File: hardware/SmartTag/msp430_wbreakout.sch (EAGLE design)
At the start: 19 parts, among them U1 ADXL362

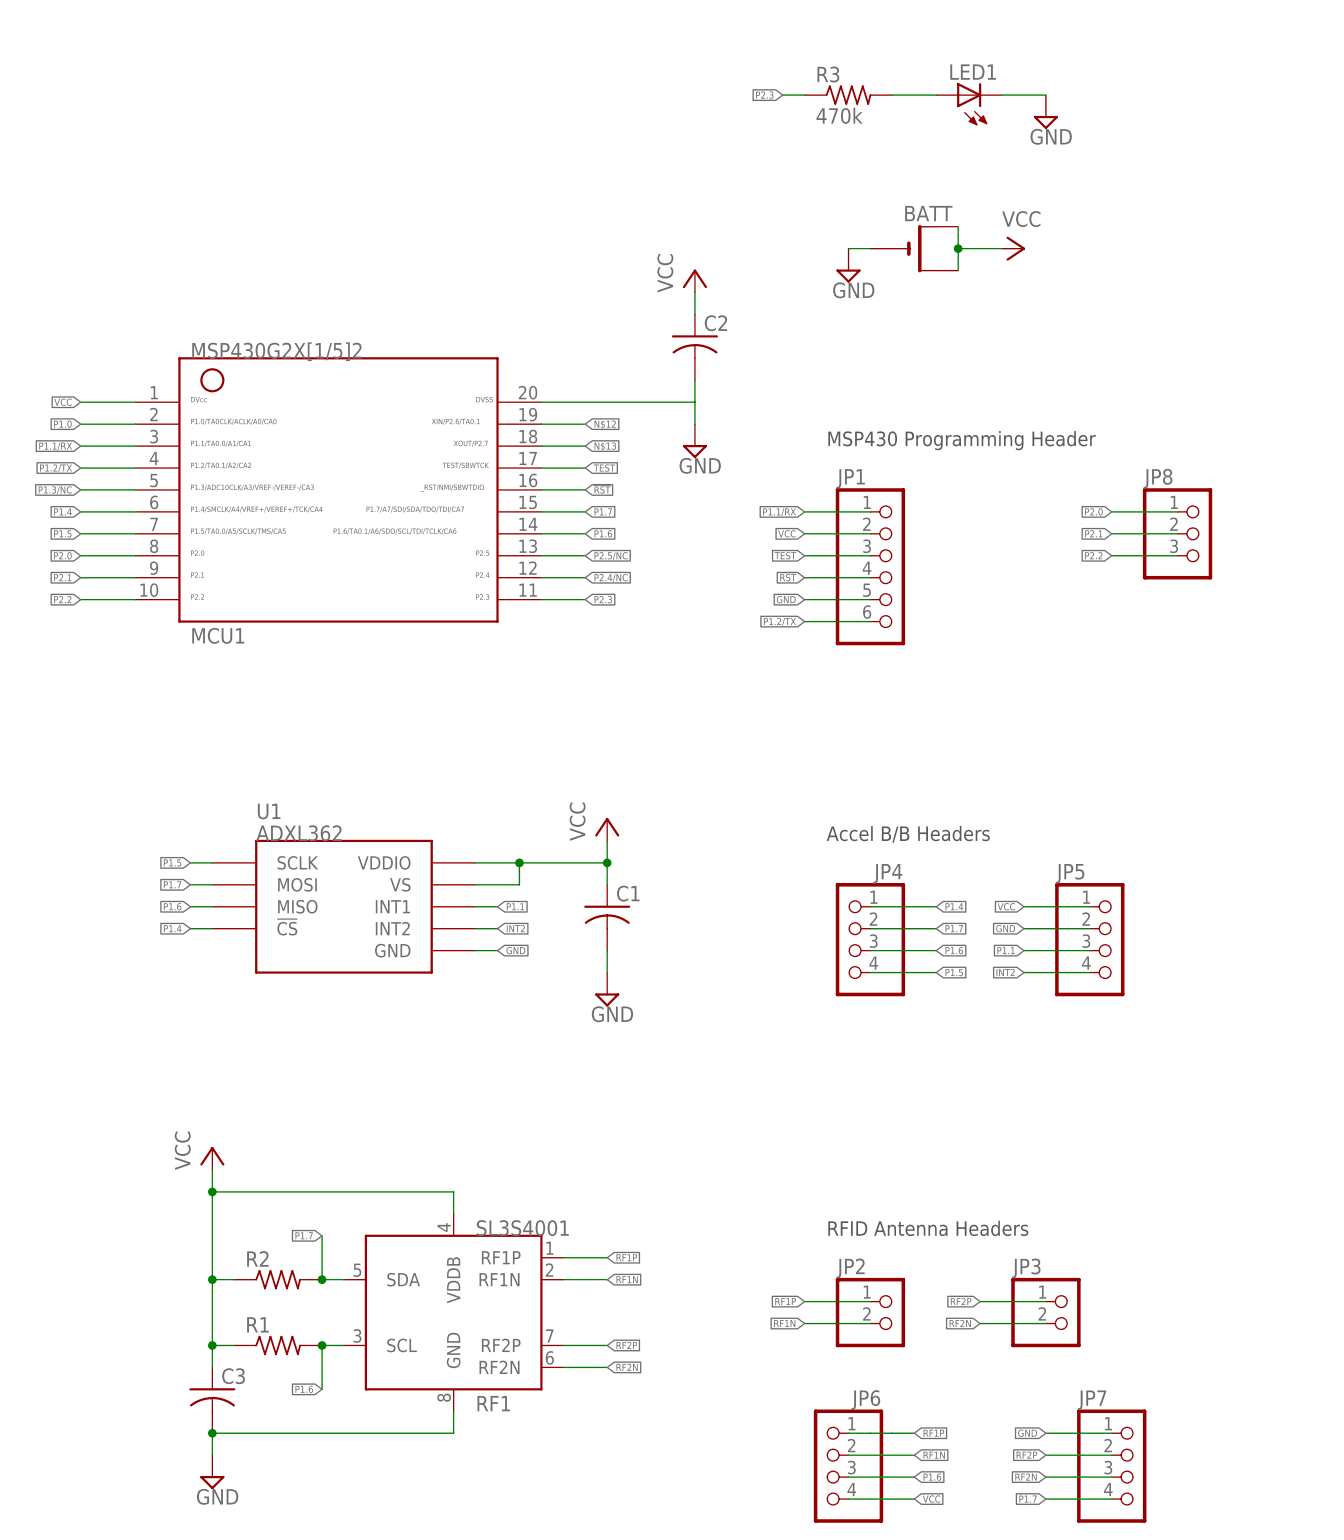
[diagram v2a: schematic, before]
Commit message: hw: Update based on 1/29 Meeting Notes
Added pin header for Bluetooth board.
Added RESET switch.
Rearranged traces for capacitive sensor connections.

Passed DRC and ERC using SparkFun "Tight" rules
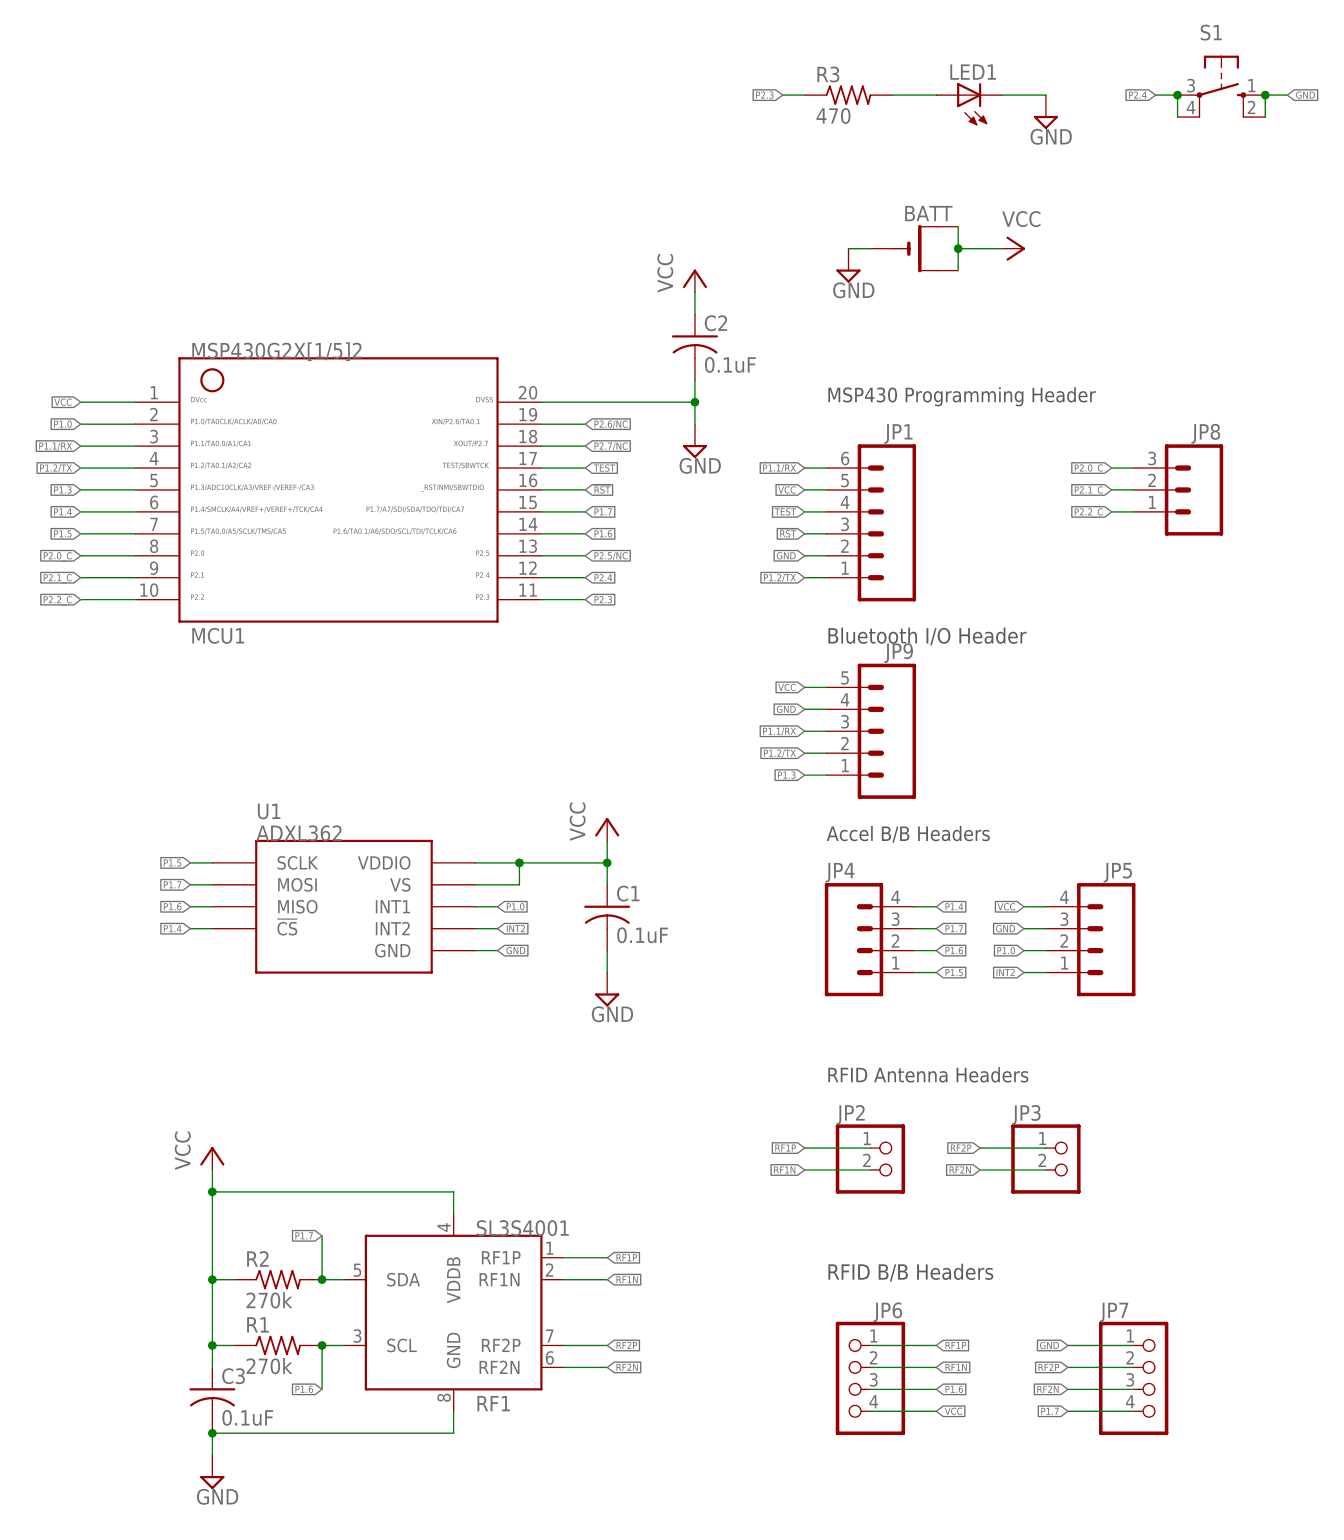
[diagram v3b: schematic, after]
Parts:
- added JP9: (no value), SparkFun-Connectors:M05LOCK
- added S1: (no value), switch-omron:10-XX
- C1, C2, C3: value (none) -> 0.1uF
- JP1: device pinhead:PINHD-1X6 -> SparkFun-Connectors:M06LOCK
- JP4, JP5: device pinhead:PINHD-1X4 -> SparkFun-Connectors:M04LOCK
- JP8: device pinhead:PINHD-1X3 -> SparkFun-Connectors:M03LOCK
- R1, R2: value (none) -> 270k
- R3: value 470k -> 470
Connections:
- net N$12 renamed P2.6/NC
- net N$13 renamed P2.7/NC
- net P2.1 renamed P2.1_C
- removed net P1.1: JP5.3, U1.INT1
- removed net P1.3/NC: MCU1.5
- removed net P2.0: JP8.1, MCU1.8
- removed net P2.2: JP8.3, MCU1.10
- removed net P2.4/NC: MCU1.12
- new net P1.3: JP9.1, MCU1.5
- new net P2.0_C: JP8.3, MCU1.8
- new net P2.2_C: JP8.1, MCU1.10
- new net P2.4: MCU1.12, S1.P, S1.P1
- net !RST: now also JP1.3; no longer JP1.4
- net GND: now also JP1.2, JP5.3, JP9.4, S1.S, S1.S1; no longer JP1.5, JP5.2
- net INT2: now also JP5.1; no longer JP5.4
- net P1.0: now also JP5.2, U1.INT1
- net P1.1/RX: now also JP1.6, JP9.3; no longer JP1.1
- net P1.2/TX: now also JP1.1, JP9.2; no longer JP1.6
- net P1.4: now also JP4.4; no longer JP4.1
- net P1.5: now also JP4.1; no longer JP4.4
- net P1.6: now also JP4.2; no longer JP4.3
- net P1.7: now also JP4.3; no longer JP4.2
- net TEST: now also JP1.4; no longer JP1.3
- net VCC: now also JP1.5, JP5.4, JP9.5; no longer JP1.2, JP5.1
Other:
- note added: "Bluetooth I/O Header"
- note added: "RFID B/B Headers"
- moved on the sheet: JP2, JP3, JP6, JP7
